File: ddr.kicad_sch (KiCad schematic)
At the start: 4 parts, among them U3 MT40A1G16KD-062E

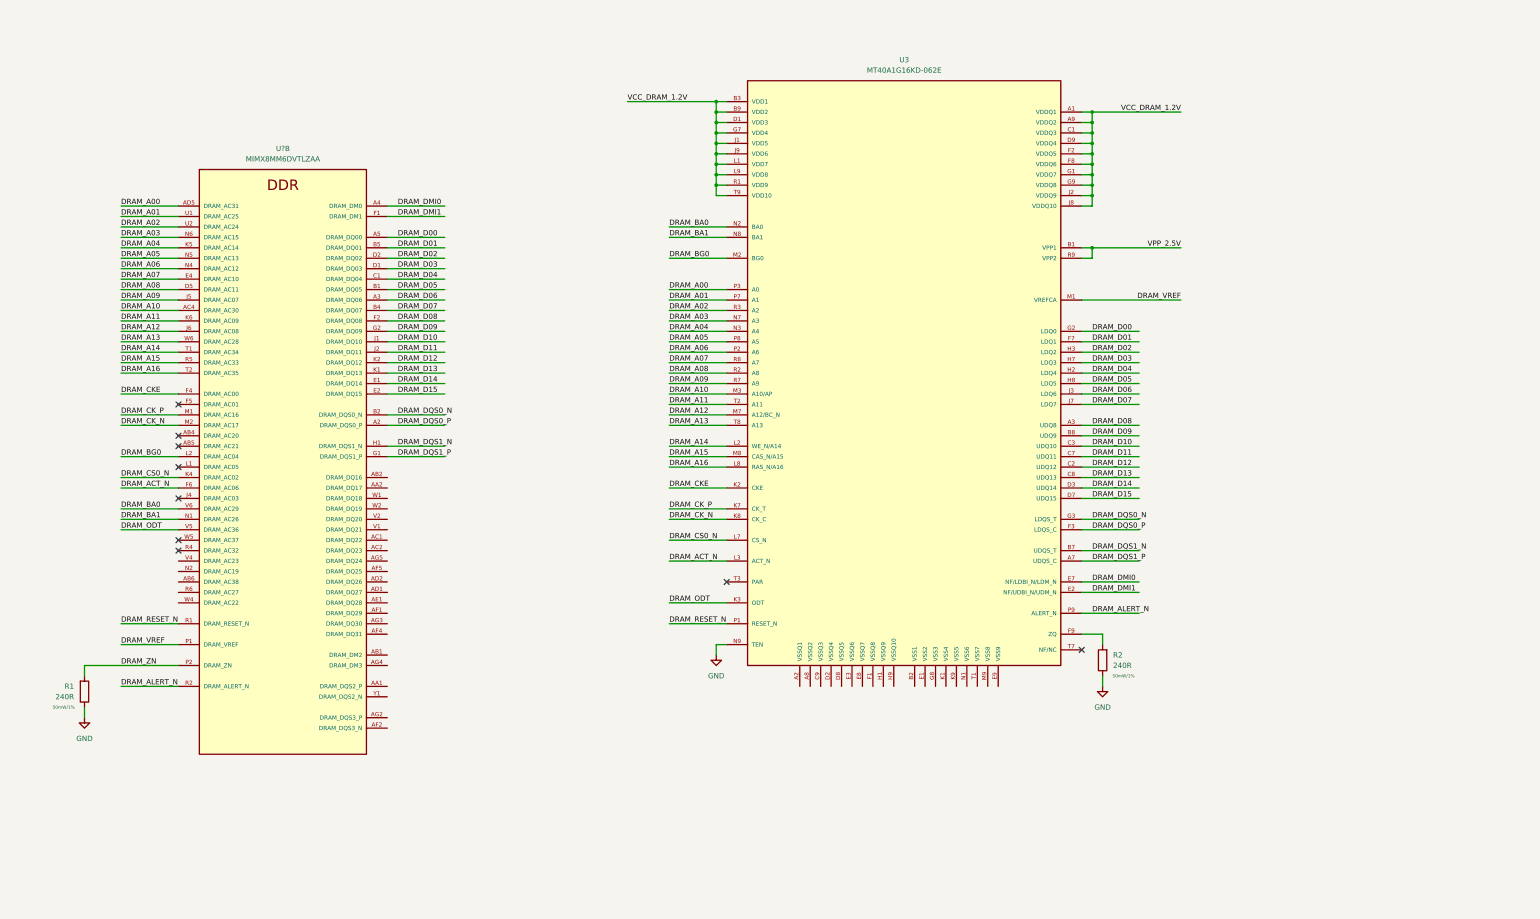
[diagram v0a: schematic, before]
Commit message: ddr sch done
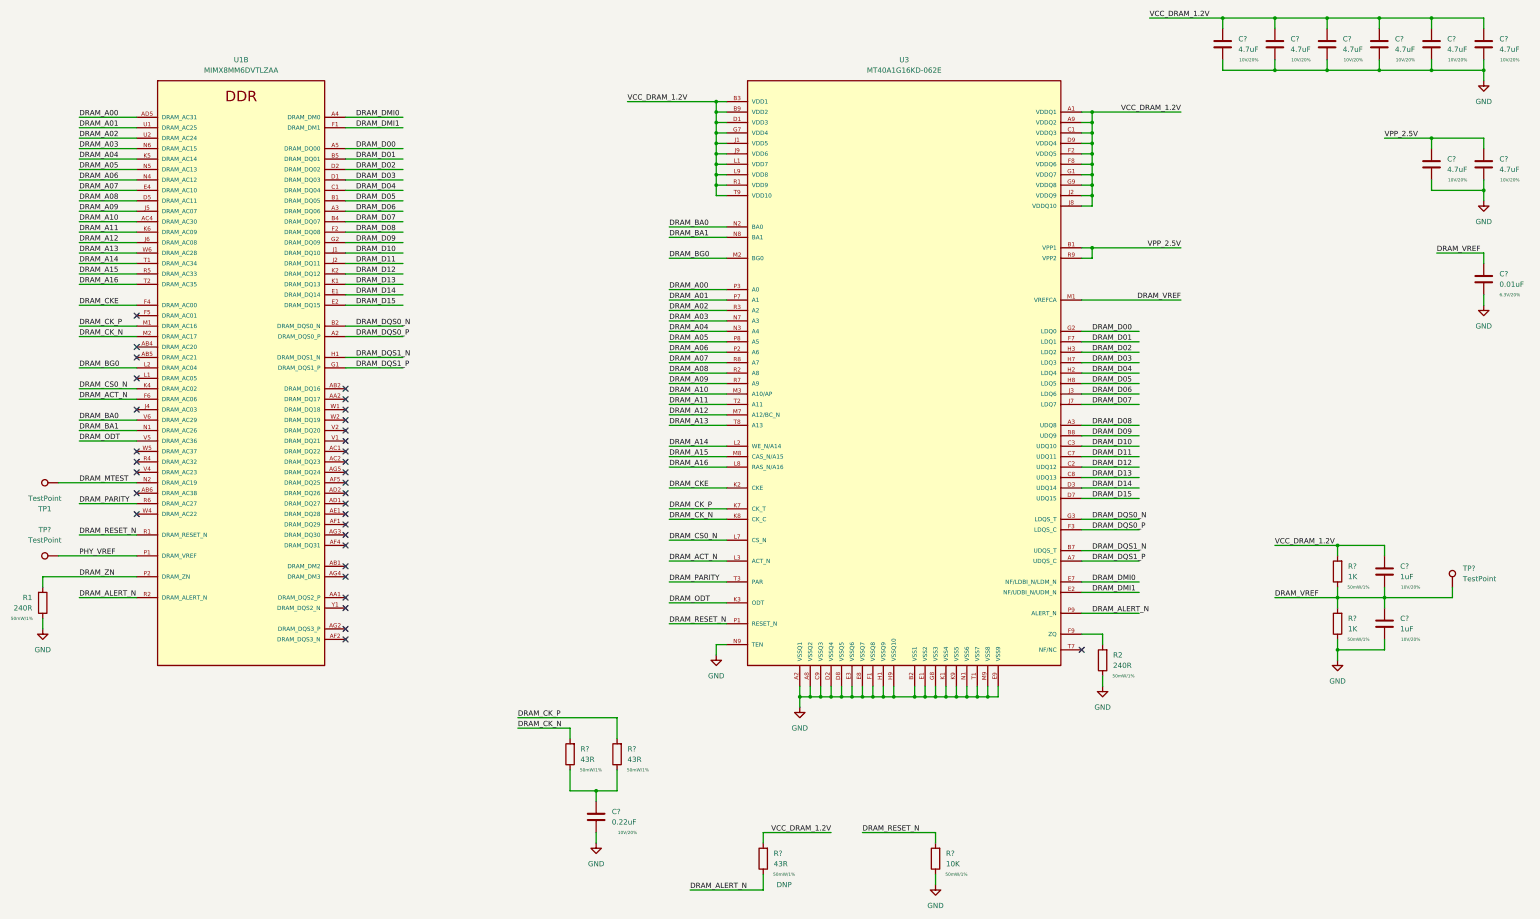
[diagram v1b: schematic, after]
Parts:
- added C? (x8): 4.7uF, Capacitor_SMD:C_0402_1005Metric, symbol Device:C
- added C? (x2): 1uF, Capacitor_SMD:C_0402_1005Metric, symbol Device:C
- added C?: 0.22uF, Capacitor_SMD:C_0201_0603Metric, symbol Device:C
- added C?: 0.01uF, Capacitor_SMD:C_0201_0603Metric, symbol Device:C
- added R? (x3): 43R, Resistor_SMD:R_0201_0603Metric, symbol Device:R
- added R?: 10K, Resistor_SMD:R_0402_1005Metric, symbol Device:R
- added R? (x2): 1K, Resistor_SMD:R_0402_1005Metric, symbol Device:R
- added TP1, TP? (x2): TestPoint, TestPoint:TestPoint_Pad_D1.0mm, symbol Connector:TestPoint
- gave numbers to parts that had none: 1
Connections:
- net DRAM_ALERT_N: now also R?.1
- net DRAM_CK_N: now also R?.2
- net DRAM_CK_P: now also R?.2
- net DRAM_RESET_N: now also R?.2
- net DRAM_VREF: now also C?.1, C?.1, C?.2, R?.1, R?.2, TP?.1; no longer U1.P1 (DRAM_VREF)
- net GND: now also U3.A2 (VSSQ1), U3.A8 (VSSQ2), U3.B2 (VSS1), U3.C9 (VSSQ3), U3.D2 (VSSQ4), U3.D8 (VSSQ5), U3.E1 (VSS2), U3.E3 (VSSQ6), U3.E8 (VSSQ7), U3.E9 (VSS9), U3.F1 (VSSQ8), U3.G8 (VSS3), U3.H1 (VSSQ9), U3.H9 (VSSQ10), U3.K1 (VSS4), U3.K9 (VSS5), U3.M9 (VSS8), U3.N1 (VSS6), U3.T1 (VSS7), C?.2, C?.2, C?.2, C?.2, C?.2, C?.2, C?.2, C?.2, C?.2, C?.2, C?.2, R?.1, R?.1
- net VCC_DRAM_1.2V: now also C?.1, C?.1, C?.1, C?.1, C?.1, C?.1, C?.1, R?.2, R?.2
- net VPP_2.5V: now also C?.1, C?.1
- net DRAM_MTEST: now reaches U1.N2 (DRAM_AC19)
- net DRAM_MTEST: now also TP1.1
- net DRAM_PARITY: now reaches U1.R6 (DRAM_AC27)
- net DRAM_PARITY: now also U3.T3 (PAR)
- new net: C?.1, R?.1, R?.1
- new net PHY_VREF: TP?.1, U1.P1 (DRAM_VREF)
- no-connect marks 9 -> 33
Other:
- moved on the sheet: R1, U1B

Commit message: misc work, usb sch done
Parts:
- gave numbers to parts that had none: 20
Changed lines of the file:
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@@
   (symbol (lib_id "Device:R") (at 170.18 212.09 180) (unit 1)
     (in_bom yes) (on_board yes)
-    (property "Reference" "R?" (id 0) (at 172.72 210.8199 0)
+    (property "Reference" "R3" (id 0) (at 172.72 210.8199 0)
       (effects (font (size 1.27 1.27)) (justify right))
     )
@@
   (symbol (lib_id "power:GND") (at 226.06 200.66 0) (unit 1)
     (in_bom yes) (on_board yes) (fields_autoplaced)
-    (property "Reference" "#PWR?" (id 0) (at 226.06 207.01 0)
+    (property "Reference" "#PWR0106" (id 0) (at 226.06 207.01 0)
       (effects (font (size 1.27 1.27)) hide)
     )
@@
   (symbol (lib_id "power:GND") (at 392.43 77.47 0) (unit 1)
     (in_bom yes) (on_board yes) (fields_autoplaced)
-    (property "Reference" "#PWR?" (id 0) (at 392.43 83.82 0)
+    (property "Reference" "#PWR0111" (id 0) (at 392.43 83.82 0)
       (effects (font (size 1.27 1.27)) hide)
     )
@@
   (symbol (lib_id "Device:C") (at 328.93 39.37 0) (unit 1)
     (in_bom yes) (on_board yes)
-    (property "Reference" "C?" (id 0) (at 332.74 38.0999 0)
+    (property "Reference" "C2" (id 0) (at 332.74 38.0999 0)
       (effects (font (size 1.27 1.27)) (justify left))
     )
@@
   (symbol (lib_id "Device:C") (at 354.33 39.37 0) (unit 1)
     (in_bom yes) (on_board yes)
-    (property "Reference" "C?" (id 0) (at 358.14 38.0999 0)
+    (property "Reference" "C4" (id 0) (at 358.14 38.0999 0)
       (effects (font (size 1.27 1.27)) (justify left))
     )
@@
   (symbol (lib_id "Connector:TestPoint") (at 45.72 163.83 90) (mirror x) (unit 1)
     (in_bom yes) (on_board yes)
-    (property "Reference" "TP?" (id 0) (at 42.418 157.48 90))
+    (property "Reference" "TP2" (id 0) (at 42.418 157.48 90))
     (property "Value" "TestPoint" (id 1) (at 42.418 160.02 90))
     (property "Footprint" "TestPoint:TestPoint_Pad_D1.0mm" (id 2) (at 45.72 168.91 0)
@@
   (symbol (lib_id "Device:R") (at 217.17 237.49 180) (unit 1)
     (in_bom yes) (on_board yes)
-    (property "Reference" "R?" (id 0) (at 219.71 236.2199 0)
+    (property "Reference" "R5" (id 0) (at 219.71 236.2199 0)
       (effects (font (size 1.27 1.27)) (justify right))
     )
@@
   (symbol (lib_id "Device:R") (at 259.08 237.49 180) (unit 1)
     (in_bom yes) (on_board yes)
-    (property "Reference" "R?" (id 0) (at 261.62 236.2199 0)
+    (property "Reference" "R6" (id 0) (at 261.62 236.2199 0)
       (effects (font (size 1.27 1.27)) (justify right))
     )
@@
   (symbol (lib_id "Device:C") (at 368.3 180.34 0) (unit 1)
     (in_bom yes) (on_board yes)
-    (property "Reference" "C?" (id 0) (at 372.11 179.0699 0)
+    (property "Reference" "C7" (id 0) (at 372.11 179.0699 0)
       (effects (font (size 1.27 1.27)) (justify left))
     )
@@
   (symbol (lib_id "Device:C") (at 341.63 39.37 0) (unit 1)
     (in_bom yes) (on_board yes)
-    (property "Reference" "C?" (id 0) (at 345.44 38.0999 0)
+    (property "Reference" "C3" (id 0) (at 345.44 38.0999 0)
       (effects (font (size 1.27 1.27)) (justify left))
     )
@@
   (symbol (lib_id "Connector:TestPoint") (at 384.81 171.45 0) (unit 1)
     (in_bom yes) (on_board yes) (fields_autoplaced)
-    (property "Reference" "TP?" (id 0) (at 387.35 166.8779 0)
+    (property "Reference" "TP3" (id 0) (at 387.35 166.8779 0)
       (effects (font (size 1.27 1.27)) (justify left))
     )
@@
   (symbol (lib_id "Device:C") (at 392.43 39.37 0) (unit 1)
     (in_bom yes) (on_board yes)
-    (property "Reference" "C?" (id 0) (at 396.24 38.0999 0)
+    (property "Reference" "C10" (id 0) (at 396.24 38.0999 0)
       (effects (font (size 1.27 1.27)) (justify left))
     )
@@
   (symbol (lib_id "power:GND") (at 176.53 233.68 0) (unit 1)
     (in_bom yes) (on_board yes) (fields_autoplaced)
-    (property "Reference" "#PWR?" (id 0) (at 176.53 240.03 0)
+    (property "Reference" "#PWR0108" (id 0) (at 176.53 240.03 0)
       (effects (font (size 1.27 1.27)) hide)
     )
@@
   (symbol (lib_id "Device:R") (at 356.87 167.64 180) (unit 1)
     (in_bom yes) (on_board yes)
-    (property "Reference" "R?" (id 0) (at 359.41 166.3699 0)
+    (property "Reference" "R7" (id 0) (at 359.41 166.3699 0)
       (effects (font (size 1.27 1.27)) (justify right))
     )
@@
   (symbol (lib_id "power:GND") (at 392.43 102.87 0) (unit 1)
     (in_bom yes) (on_board yes) (fields_autoplaced)
-    (property "Reference" "#PWR?" (id 0) (at 392.43 109.22 0)
+    (property "Reference" "#PWR0112" (id 0) (at 392.43 109.22 0)
       (effects (font (size 1.27 1.27)) hide)
     )
@@
   (symbol (lib_id "Device:C") (at 176.53 227.33 0) (unit 1)
     (in_bom yes) (on_board yes)
-    (property "Reference" "C?" (id 0) (at 180.34 226.0599 0)
+    (property "Reference" "C1" (id 0) (at 180.34 226.0599 0)
       (effects (font (size 1.27 1.27)) (justify left))
     )
@@
   (symbol (lib_id "Device:R") (at 356.87 180.34 180) (unit 1)
     (in_bom yes) (on_board yes)
-    (property "Reference" "R?" (id 0) (at 359.41 179.0699 0)
+    (property "Reference" "R8" (id 0) (at 359.41 179.0699 0)
       (effects (font (size 1.27 1.27)) (justify right))
     )
@@
   (symbol (lib_id "power:GND") (at 392.43 48.26 0) (unit 1)
     (in_bom yes) (on_board yes) (fields_autoplaced)
-    (property "Reference" "#PWR?" (id 0) (at 392.43 54.61 0)
+    (property "Reference" "#PWR0110" (id 0) (at 392.43 54.61 0)
       (effects (font (size 1.27 1.27)) hide)
     )
@@
   (symbol (lib_id "Device:C") (at 392.43 68.58 0) (unit 1)
     (in_bom yes) (on_board yes)
-    (property "Reference" "C?" (id 0) (at 396.24 67.3099 0)
+    (property "Reference" "C11" (id 0) (at 396.24 67.3099 0)
       (effects (font (size 1.27 1.27)) (justify left))
     )
@@
   (symbol (lib_id "Device:C") (at 379.73 39.37 0) (unit 1)
     (in_bom yes) (on_board yes)
-    (property "Reference" "C?" (id 0) (at 383.54 38.0999 0)
+    (property "Reference" "C8" (id 0) (at 383.54 38.0999 0)
       (effects (font (size 1.27 1.27)) (justify left))
     )
@@
   (symbol (lib_id "Device:C") (at 379.73 68.58 0) (unit 1)
     (in_bom yes) (on_board yes)
-    (property "Reference" "C?" (id 0) (at 383.54 67.3099 0)
+    (property "Reference" "C9" (id 0) (at 383.54 67.3099 0)
       (effects (font (size 1.27 1.27)) (justify left))
     )
@@
   (symbol (lib_id "Device:C") (at 392.43 96.52 0) (unit 1)
     (in_bom yes) (on_board yes)
-    (property "Reference" "C?" (id 0) (at 396.24 95.2499 0)
+    (property "Reference" "C12" (id 0) (at 396.24 95.2499 0)
       (effects (font (size 1.27 1.27)) (justify left))
     )
@@
   (symbol (lib_id "power:GND") (at 259.08 243.84 0) (unit 1)
     (in_bom yes) (on_board yes) (fields_autoplaced)
-    (property "Reference" "#PWR?" (id 0) (at 259.08 250.19 0)
+    (property "Reference" "#PWR0107" (id 0) (at 259.08 250.19 0)
       (effects (font (size 1.27 1.27)) hide)
     )
@@
   (symbol (lib_id "Device:C") (at 368.3 167.64 0) (unit 1)
     (in_bom yes) (on_board yes)
-    (property "Reference" "C?" (id 0) (at 372.11 166.3699 0)
+    (property "Reference" "C6" (id 0) (at 372.11 166.3699 0)
       (effects (font (size 1.27 1.27)) (justify left))
     )
@@
   (symbol (lib_id "Device:C") (at 367.03 39.37 0) (unit 1)
     (in_bom yes) (on_board yes)
-    (property "Reference" "C?" (id 0) (at 370.84 38.0999 0)
+    (property "Reference" "C5" (id 0) (at 370.84 38.0999 0)
       (effects (font (size 1.27 1.27)) (justify left))
     )
@@
   (symbol (lib_id "Device:R") (at 181.61 212.09 180) (unit 1)
     (in_bom yes) (on_board yes)
-    (property "Reference" "R?" (id 0) (at 184.15 210.8199 0)
+    (property "Reference" "R4" (id 0) (at 184.15 210.8199 0)
       (effects (font (size 1.27 1.27)) (justify right))
     )
@@
   (symbol (lib_id "power:GND") (at 356.87 189.23 0) (unit 1)
     (in_bom yes) (on_board yes) (fields_autoplaced)
-    (property "Reference" "#PWR?" (id 0) (at 356.87 195.58 0)
-      (effects (font (size 1.27 1.27)) hide)
-    )
+    (property "Reference" "#PWR0109" (id 0) (at 356.87 195.58 0)
+      (effects (font (size 1.27 1.27)) hide)
+    )
